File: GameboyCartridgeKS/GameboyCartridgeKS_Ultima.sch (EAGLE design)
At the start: 27 parts, among them IC1 AT49F040J

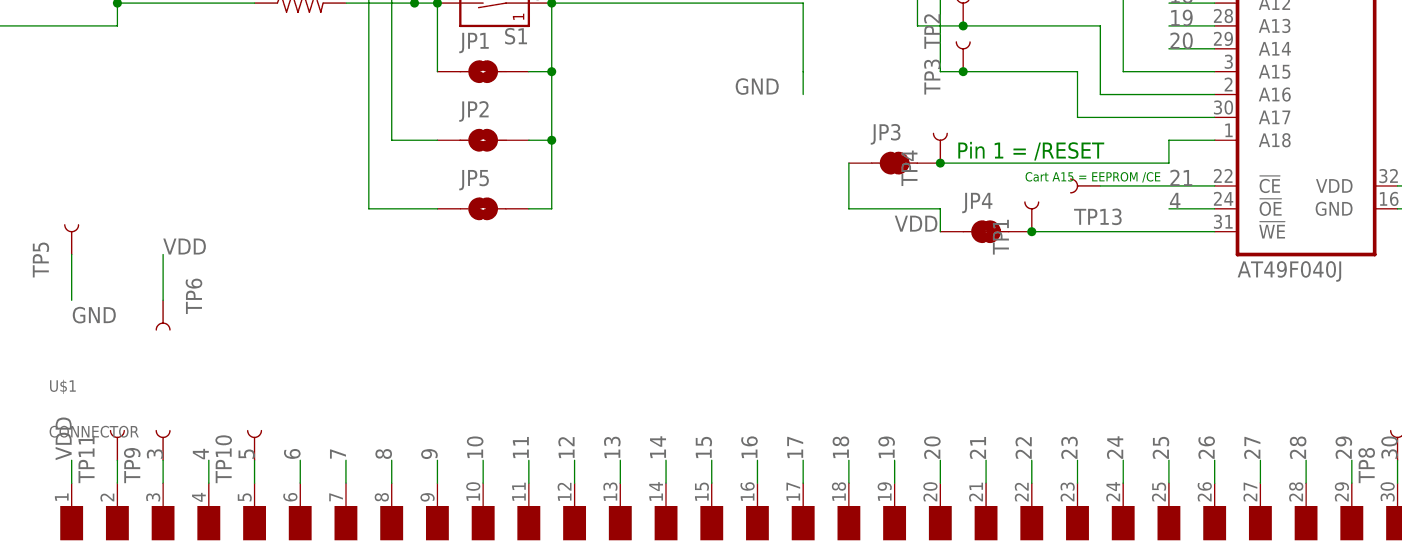
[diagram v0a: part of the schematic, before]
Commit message: Added solderpad for the RD signal, and the post-migration missing gitignore file
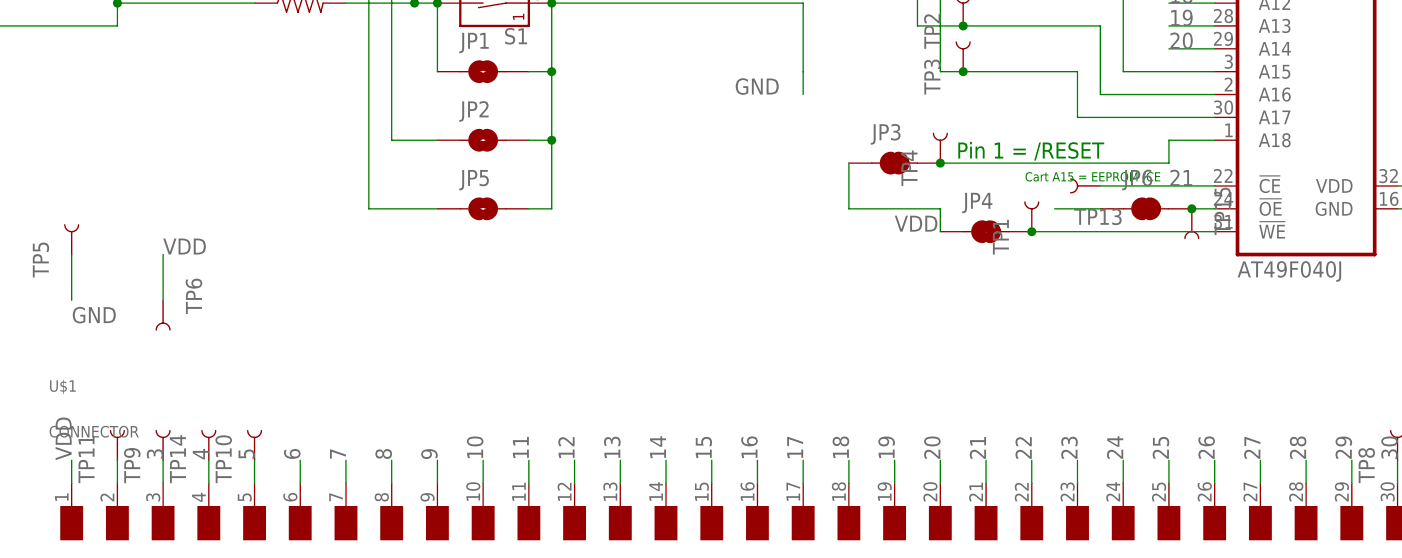
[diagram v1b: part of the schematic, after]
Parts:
- added JP6: JUMPER-SMT_2_NC_TRACE_SILK, SparkFun-Jumpers:JUMPER-SMT_2_NC_TRACE_SILK
- added TP14, TP15: TEST-POINT3X5, SparkFun-Connectors:TEST-POINT3X5
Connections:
- new net N$3: IC1.!OE, JP6.2, TP15.1
- net 4: now also JP6.1, TP14.1; no longer IC1.!OE
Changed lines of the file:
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@@
 <part name="JP2" library="SparkFun-Jumpers" deviceset="JUMPER-SMT_2_NO" device="_NO-SILK" package3d_urn="urn:adsk.eagle:package:39277/1"/>
 <part name="JP5" library="SparkFun-Jumpers" deviceset="JUMPER-SMT_2_NO" device="_NO-SILK" package3d_urn="urn:adsk.eagle:package:39277/1"/>
+<part name="TP14" library="SparkFun-Connectors" library_urn="urn:adsk.eagle:library:513" deviceset="TEST-POINT" device="3X5" package3d_urn="urn:adsk.eagle:package:38285/1"/>
+<part name="JP6" library="SparkFun-Jumpers" deviceset="JUMPER-SMT_2_NC_TRACE" device="_SILK" package3d_urn="urn:adsk.eagle:package:39281/1"/>
+<part name="TP15" library="SparkFun-Connectors" library_urn="urn:adsk.eagle:library:513" deviceset="TEST-POINT" device="3X5" package3d_urn="urn:adsk.eagle:package:38285/1"/>
 </parts>
 <sheets>
@@
 <instance part="JP5" gate="G$1" x="38.1" y="83.82" smashed="yes">
 <attribute name="NAME" x="35.56" y="86.36" size="1.778" layer="95" font="vector"/>
+</instance>
+<instance part="TP14" gate="G$1" x="7.62" y="55.88" smashed="yes" rot="R90">
+<attribute name="NAME" x="5.08" y="53.34" size="1.778" layer="95" font="vector" rot="R90"/>
+</instance>
+<instance part="JP6" gate="G$1" x="111.76" y="83.82" smashed="yes">
+<attribute name="NAME" x="109.22" y="86.36" size="1.778" layer="95" font="vector"/>
+</instance>
+<instance part="TP15" gate="G$1" x="116.84" y="83.82" smashed="yes" rot="R270">
+<attribute name="NAME" x="119.38" y="86.36" size="1.778" layer="95" font="vector" rot="R270"/>
 </instance>
 </instances>
@@
 <wire x1="7.62" y1="53.34" x2="7.62" y2="55.88" width="0.1524" layer="91"/>
 <label x="7.62" y="55.88" size="1.778" layer="95" rot="R90"/>
-</segment>
-<segment>
-<pinref part="IC1" gate="G$1" pin="!OE"/>
-<wire x1="119.38" y1="83.82" x2="114.3" y2="83.82" width="0.1524" layer="91"/>
-<label x="114.3" y="83.82" size="1.778" layer="95"/>
+<pinref part="TP14" gate="G$1" pin="1"/>
+</segment>
+<segment>
+<pinref part="JP6" gate="G$1" pin="1"/>
+<wire x1="106.68" y1="83.82" x2="101.6" y2="83.82" width="0.1524" layer="91"/>
 </segment>
 </net>
@@
 </segment>
 </net>
+<net name="N$3" class="0">
+<segment>
+<pinref part="IC1" gate="G$1" pin="!OE"/>
+<pinref part="JP6" gate="G$1" pin="2"/>
+<wire x1="116.84" y1="83.82" x2="119.38" y2="83.82" width="0.1524" layer="91"/>
+<pinref part="TP15" gate="G$1" pin="1"/>
+<junction x="116.84" y="83.82"/>
+</segment>
+</net>
